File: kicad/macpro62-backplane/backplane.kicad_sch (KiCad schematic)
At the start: 0 parts

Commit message: Cross-board compatibility audit: interface control doc, CR-BP-1 applied, J2/J3 row-swap pinouts, 15-pin face AUX, fan header removed from backplane, CPU board i226/BT1 cleanup
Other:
- removed sheet Fan
- sheet CPU board link (J1 CPU-LINK card edge) ports: added IOB_USB_DN, IOB_USB_DP, MOD_I2C0_SCL, MOD_I2C0_SDA; removed none
- sheet Face P (primary) AUX link ports: added FACE_MOD_LED_N; removed none
- sheet Face S (secondary) AUX link ports: added FACE_MOD_LED_N; removed none
- sheet I/O board low-speed link ports: added IOB_INT_N, IOB_PRSNT_N, IOB_USB_DN, IOB_USB_DP; removed none
- sheet Management MCU (RP2350A) ports: added FACE_P_MOD_LED_N, FACE_S_MOD_LED_N, IOB_INT_N, IOB_PRSNT_N, MOD_I2C0_SCL, MOD_I2C0_SDA; removed FAN_PWM, FAN_TACH
- sheet Power input, standby rails, safety gate ports: added none; removed 11V_SB, 12V_MAIN
- note added: "Off-board links: J1 CPU-LINK (card edge from CPU board) | J2 PSU-IN | J3/J4 Face P/S AUX (GH15) | J6 IOB-LINK (fan via IOB CONN_C, no J5) | J7 M.2 OpenCore | J8 SWD | J9/J10 MCIO 124 to Face P/S (PCIe hub)"
- note removed: "Off-board links: J1 CPU-LINK (card edge from CPU board) | J2 PSU-IN | J3/J4 Face P/S AUX | J5 FAN | J6 IOB-LINK | J7 M.2 OpenCore | J8 SWD | J9/J10 MCIO 124 to Face P/S (PCIe hub)"

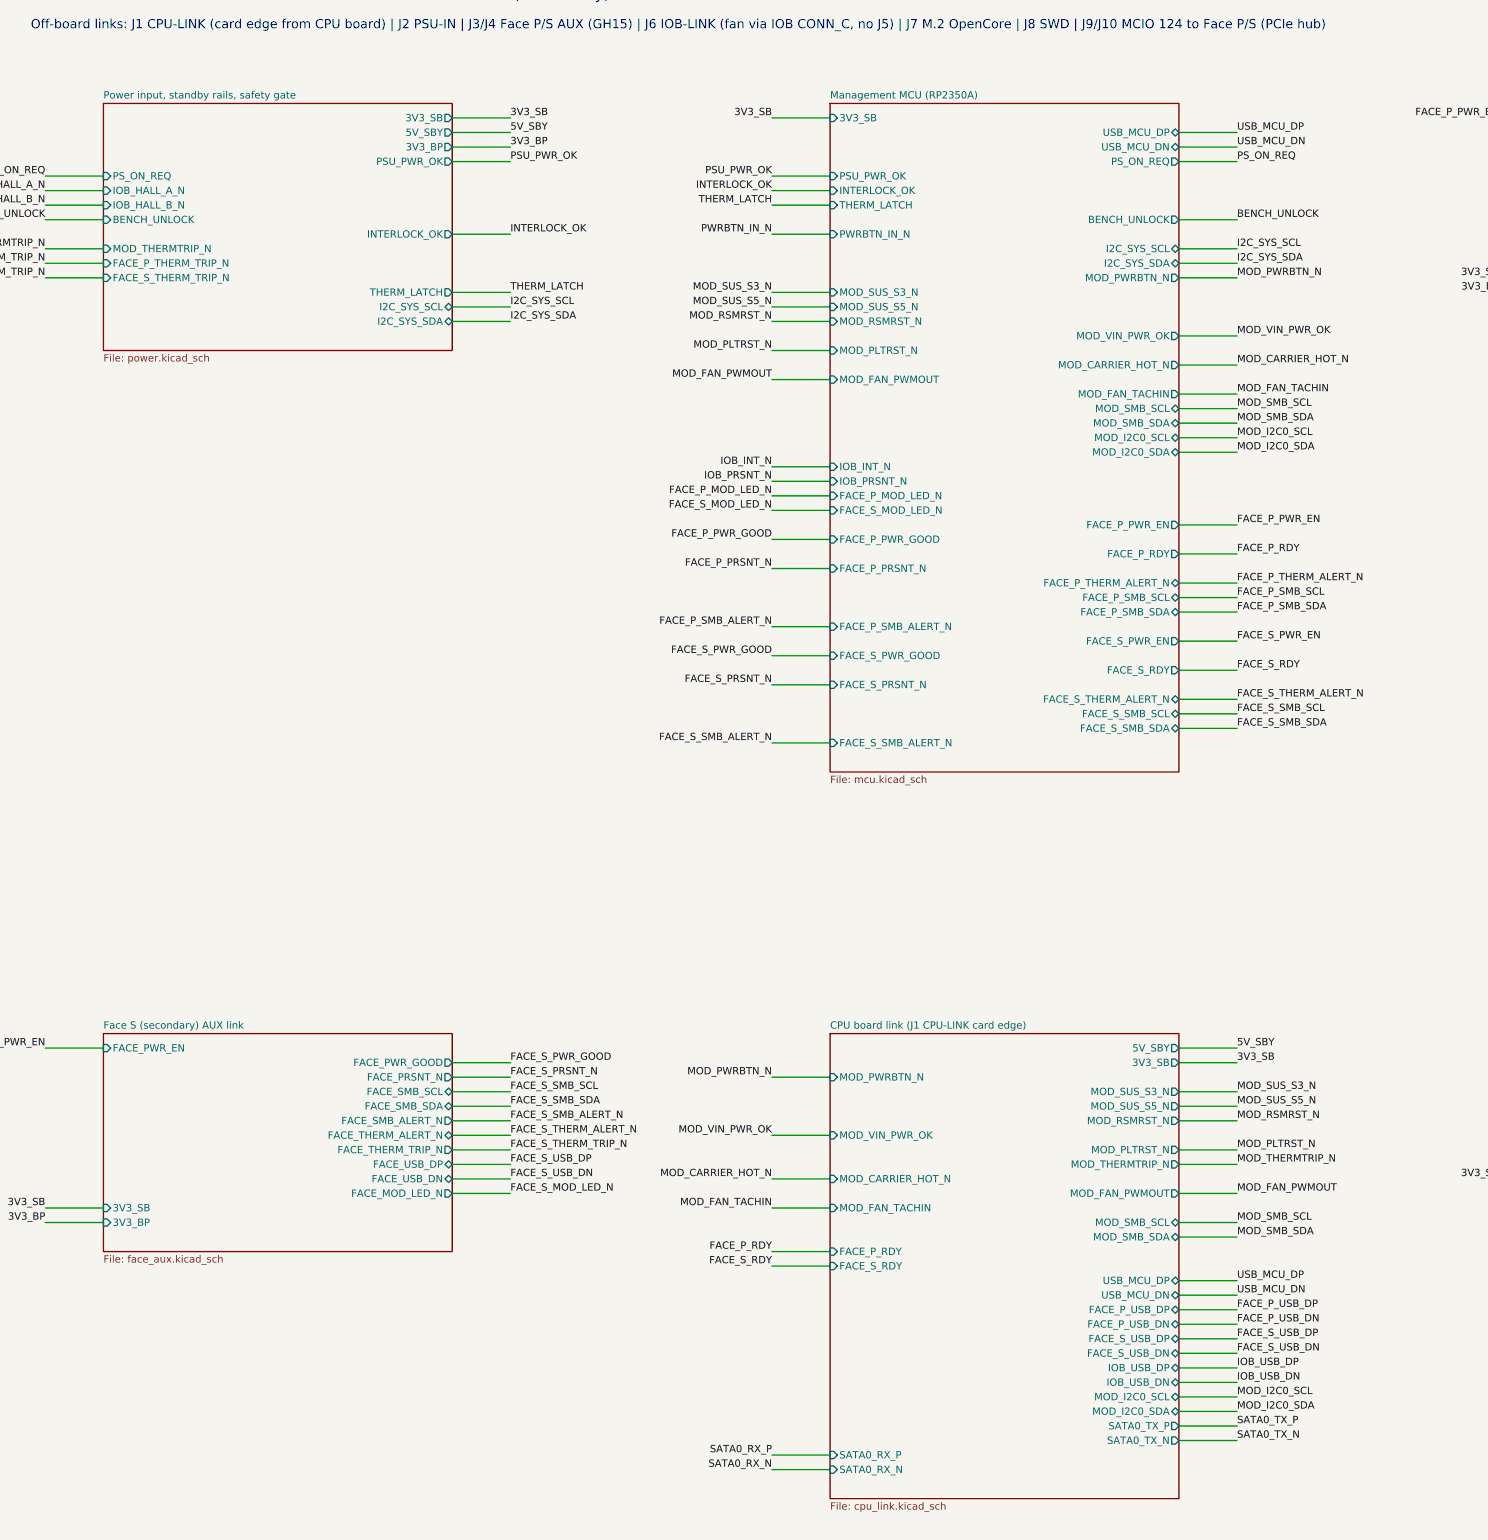
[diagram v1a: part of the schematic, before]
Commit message: ICD rev 2: 45 deg faces, 445 W ceiling + live power target (INA228 telemetry), ribbon MCIO jog cables, BT on S0, fan fail-safe, port-module I2C map
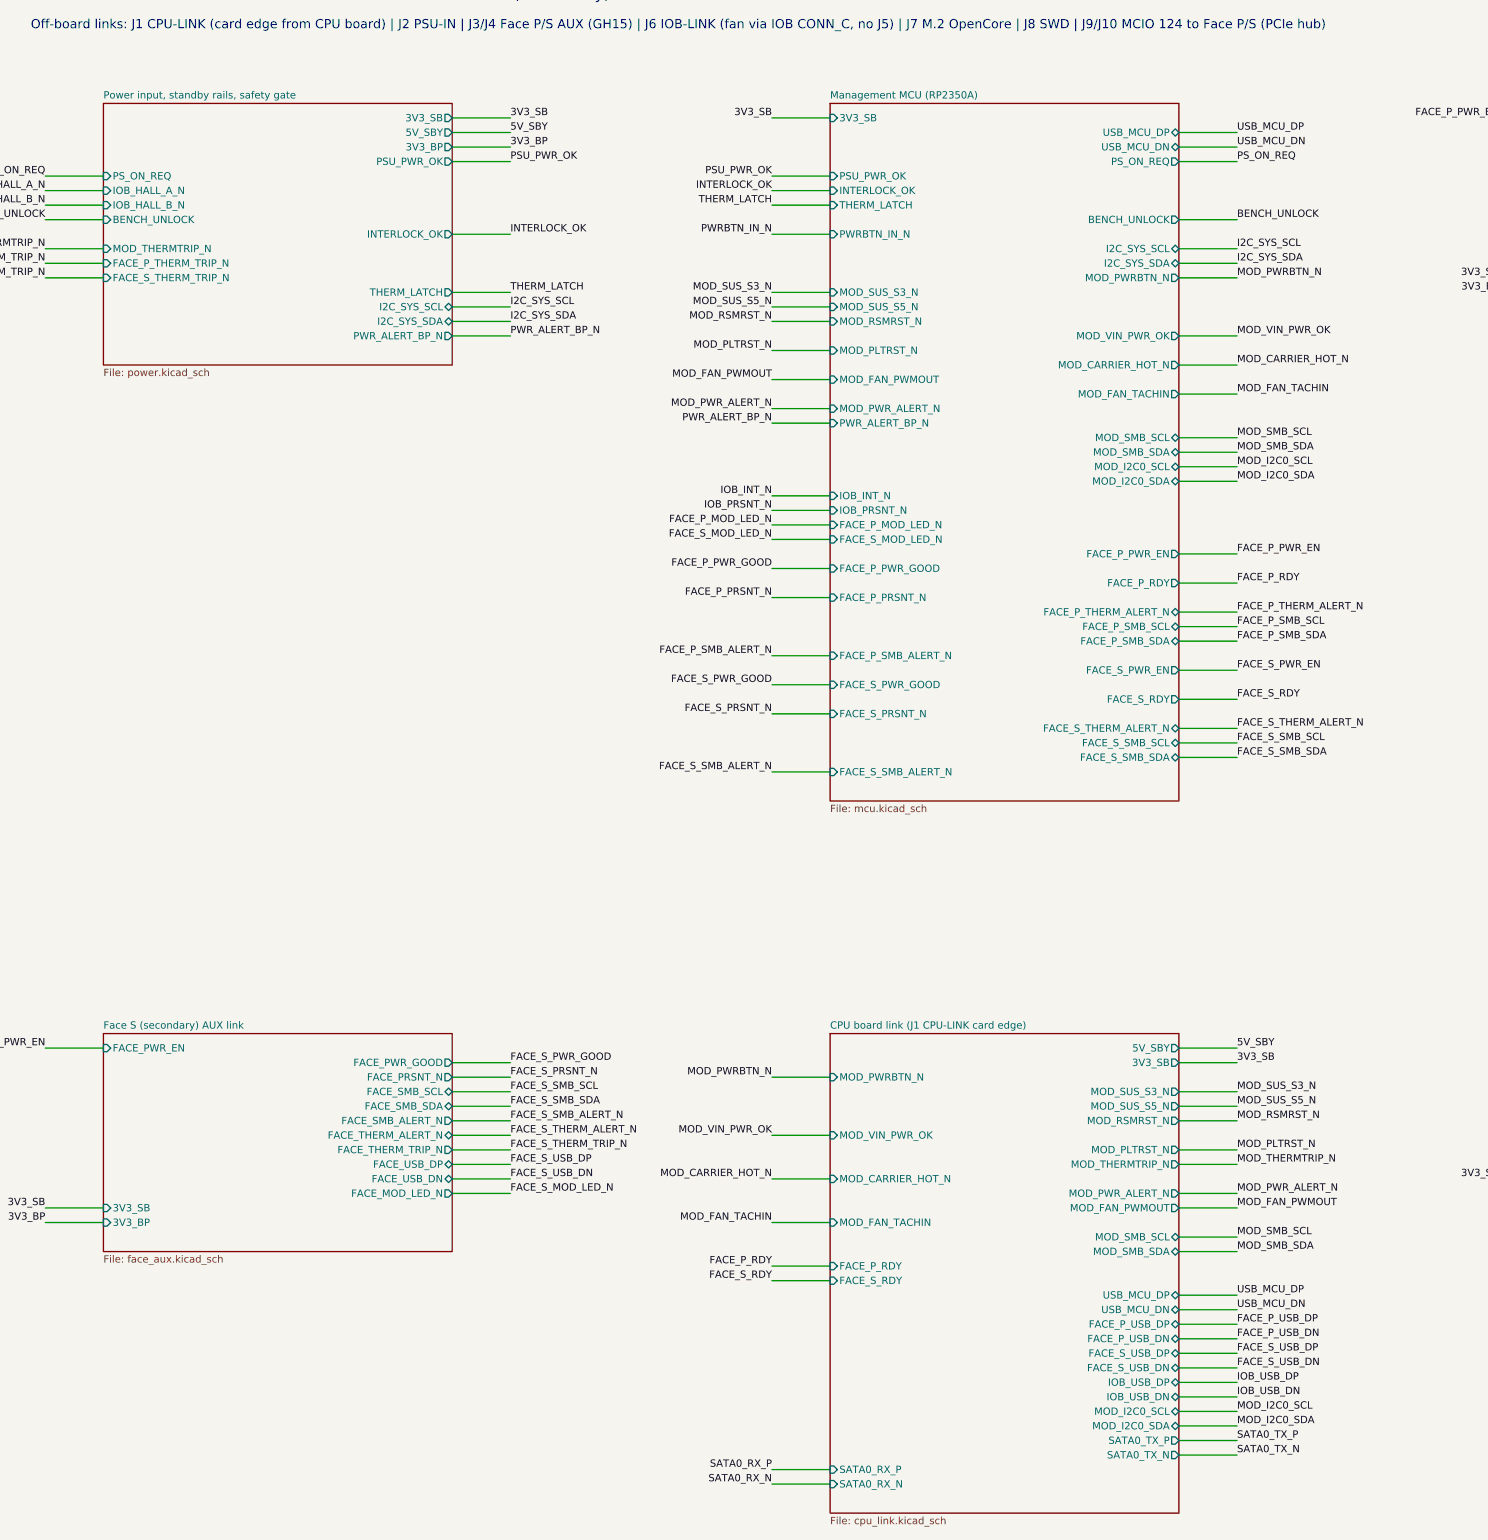
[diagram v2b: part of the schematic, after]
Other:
- sheet CPU board link (J1 CPU-LINK card edge) ports: added MOD_PWR_ALERT_N; removed none
- sheet Management MCU (RP2350A) ports: added MOD_PWR_ALERT_N, PWR_ALERT_BP_N; removed none
- sheet Power input, standby rails, safety gate ports: added PWR_ALERT_BP_N; removed none

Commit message: Backplane rev A1: 4-layer JLC04161H-7628, Gen5 redrivers removed, RP2350B MCU + INA226, fully routed (DRC/ERC 0, all HS/SATA pairs 0 skew), USB2 skew touch-up, JLC outputs
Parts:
- added C1, C12, C14, C16, C18, C19, C21, C22, C23, C24, C25, C26, C27, C28, C32, C33, C34, C35, C38, C39, C5, C8, C9: 100nF 16V X7R 0402, MP62_BP:C_0402_1005Metric, symbol MP62_BP:C
- added C10, C11, C13, C15, C17, C2, C3, C4, C6, C7: 22uF 25V X5R 0805, MP62_BP:C_0805_2012Metric, symbol MP62_BP:C
- added C20: 1uF 25V X5R 0402, MP62_BP:C_0402_1005Metric, symbol MP62_BP:C
- added C29, C30, C31: 4.7uF 10V X5R 0402, MP62_BP:C_0402_1005Metric, symbol MP62_BP:C
- added C36, C37: 15pF 50V C0G 0402, MP62_BP:C_0402_1005Metric, symbol MP62_BP:C
- added D1, D2: SS34 3A 40V Schottky SMA, MP62_BP:D_SMA, symbol MP62_BP:D
- added D10, D6, D7, D8, D9: LED red 0603, MP62_BP:LED_0603_1608Metric, symbol MP62_BP:LED
- added D3: SMAJ15A TVS SMA, MP62_BP:D_SMA, symbol MP62_BP:D
- added D4, D5: BAT54A (LBAT54ALT1G), MP62_BP:SOT-23, symbol MP62_BP:D_x2_ACom
- added F1: 3A 1206 fast fuse (0466003.NRHF class), MP62_BP:Fuse_1206_3216Metric, symbol MP62_BP:F
- added H1, H2: MountingHole D4 plated (GND), MP62_BP:MountingHole_4mm_Pad, symbol MP62_BP:HOLE
- added H3: M.2 2242 standoff pad (DNP option), MP62_BP:MP62_M2_Standoff_SMT_M2_Pad5.0, symbol MP62_BP:HOLE
- added J1: ME1022410103011 Mini Cool Edge 224 (C4941560, 0 s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, MP62_BP:MP62_CPULINK_MiniCoolEdge_224P_Vertical_SMT_PLACEHOLDER, symbol MP62_BP:CPULINK_224
- added J10: MCIO 124P RA (C4867471) -> Face S x4, MP62_BP:MP62_MCIO_124P_RA_SFF-TA-1016, symbol MP62_BP:MCIO124_BP
- added J2: Molex 43045-0812 Micro-Fit 2x4 (C277661), MP62_BP:Molex_Micro-Fit_3.0_43045-0812_2x04_P3.00mm_Vertical, symbol MP62_BP:MICROFIT8
- added J3: BM15B-GHS-TBT (C5305069) Face P AUX, MP62_BP:JST_GH_BM15B-GHS-TBT_1x15-1MP_P1.25mm_Vertical, symbol MP62_BP:GH15_AUX
- added J4: BM15B-GHS-TBT (C5305069) Face S AUX, MP62_BP:JST_GH_BM15B-GHS-TBT_1x15-1MP_P1.25mm_Vertical, symbol MP62_BP:GH15_AUX
- added J6: BM15B-GHS-TBT (C5305069) IOB-LINK, MP62_BP:JST_GH_BM15B-GHS-TBT_1x15-1MP_P1.25mm_Vertical, symbol MP62_BP:GH15_IOB
- added J7: M.2 M-key socket LOTES APCI0107 class (C841661) -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, MP62_BP:MP62_M2_MKey_SMT_H4.2_PLACEHOLDER, symbol MP62_BP:M2_M_SATA
- added J8: BM03B-SRSS-TB SWD (DNP), MP62_BP:JST_SH_BM03B-SRSS-TB_1x03-1MP_P1.00mm_Vertical, symbol MP62_BP:SH3_SWD
- added J9: MCIO 124P RA G97R24332HR class (C4867471, 0 stock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, MP62_BP:MP62_MCIO_124P_RA_SFF-TA-1016, symbol MP62_BP:MCIO124_BP
- added JP1: BENCH: bridges the Hall interlock (open = normal), MP62_BP:SolderJumper-2_P1.3mm_Open_RoundedPad1.0x1.5mm, symbol MP62_BP:JUMPER
- added L1, L2: 4.7uH 2A 4x4 (SWPA4030S4R7MT), MP62_BP:L_Changjiang_FNR4030S, symbol MP62_BP:L
- added L3: 3.3uH 0806 (FNR201610S3R3MT, RP2350 VREG), MP62_BP:L_0805_2012Metric, symbol MP62_BP:L
- added Q1, Q2, Q3, Q5, Q6, Q7, Q8: AO3401A P-MOS, MP62_BP:SOT-23, symbol MP62_BP:PMOS
- added Q10, Q11, Q4, Q9: 2N7002 N-MOS, MP62_BP:SOT-23, symbol MP62_BP:NMOS
- added R1: 33k 1% 0402, MP62_BP:R_0402_1005Metric, symbol MP62_BP:R
- added R10, R13, R14, R15, R16, R17, R18, R19, R2, R20, R21, R23, R24, R25, R26, R29, R30, R33, R34, R35, R36, R39, R4, R40, R42, R43, R44, R45, R46, R47, R48, R49, R7, R8, R9: 10k 1% 0402, MP62_BP:R_0402_1005Metric, symbol MP62_BP:R
- added R100: 10mR 1% 1W 1206 shunt, MP62_BP:R_1206_3216Metric, symbol MP62_BP:R
- added R11, R12, R55: 100k 1% 0402, MP62_BP:R_0402_1005Metric, symbol MP62_BP:R
- added R22, R31, R32, R41, R54, R58, R60, R61: 1k 1% 0402, MP62_BP:R_0402_1005Metric, symbol MP62_BP:R
- added R27, R28, R37, R38, R50, R51, R52, R53: 2.2k 1% 0402, MP62_BP:R_0402_1005Metric, symbol MP62_BP:R
- added R3: 56k 1% 0402, MP62_BP:R_0402_1005Metric, symbol MP62_BP:R
- added R5: 100k 1% 0402 (U6 EN, always on), MP62_BP:R_0402_1005Metric, symbol MP62_BP:R
- added R56: 10k 1% 0402 (12V LED), MP62_BP:R_0402_1005Metric, symbol MP62_BP:R
- added R57: 10k 1% 0402 (11V_SB LED), MP62_BP:R_0402_1005Metric, symbol MP62_BP:R
- added R59, R62, R63: 33R 1% 0402, MP62_BP:R_0402_1005Metric, symbol MP62_BP:R
- added R6: 100k 1% 0402 (U7 off until the MCU enables 5V_SBY), MP62_BP:R_0402_1005Metric, symbol MP62_BP:R
- added SW1: BOOTSEL (TS-1187A), MP62_BP:SW_Push_1P1T_XKB_TS-1187A, symbol MP62_BP:SW
- added SW2: BENCH power button (TS-1187A), MP62_BP:SW_Push_1P1T_XKB_TS-1187A, symbol MP62_BP:SW
- added U1: RP2350B QFN-80 (C42415655), MP62_BP:QFN-80-1EP_10x10mm_P0.4mm_EP3.4x3.4mm, symbol MP62_BP:RP2350B
- added U2: W25Q128JVSIQ (C97521, basic), MP62_BP:SOIC-8_5.3x5.3mm_P1.27mm, symbol MP62_BP:W25Q_SOIC8
- added U3: TMP1075DGKR @0x48 core side (C2864807), MP62_BP:VSSOP-8_3x3mm_P0.65mm, symbol MP62_BP:TMP1075_DGK
- added U4: TMP1075DGKR @0x49 PSU side (C2864807), MP62_BP:VSSOP-8_3x3mm_P0.65mm, symbol MP62_BP:TMP1075_DGK
- added U5: INA226AIDGSR @0x40 (C49851), MP62_BP:VSSOP-10_3x3mm_P0.5mm, symbol MP62_BP:INA226
- added U6: TPS563201DDCR (C116592) -> 3V3_SB, MP62_BP:SOT-23-6, symbol MP62_BP:TPS563201
- added U7: TPS563201DDCR (C116592) -> 5V_SBY, MP62_BP:SOT-23-6, symbol MP62_BP:TPS563201
- added U8: SN74LVC1G74DCUR thermal latch (C70285), MP62_BP:VSSOP-8_2.3x2mm_P0.5mm, symbol MP62_BP:LVC1G74
- added Y1: 12MHz 3225 crystal 20pF, MP62_BP:Crystal_SMD_3225-4Pin_3.2x2.5mm, symbol MP62_BP:XTAL4
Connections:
- net 3V3_SB: now also C1.1, C19.1, C21.1, C22.1, C23.1, C24.1, C25.1, C26.1, C27.1, C28.1, C29.1, C38.1, C6.1, C7.1, D10.2 (A), J1.B107 (3V3_SB), J1.B108 (3V3_SB), J6.1 (3V3_SB), J6.2 (3V3_SB), JP1.1, L1.2, Q1.2 (S), Q2.2 (S), Q3.2 (S), Q5.2 (S), Q6.2 (S), R1.1, R13.2, R14.2, R15.2, R16.2, R17.2, R18.2, R19.2, R20.2, R21.2, R23.2, R24.2, R25.2, R33.2, R34.2, R35.2, R42.2, R43.2, R44.2, R45.2, R46.2, R47.2, R48.2, R49.2, R50.2, R51.2, R52.2, R53.2, R59.1, R7.2, R8.2, R9.2, U1.15 (IOVDD), U1.24 (IOVDD), U1.29 (IOVDD), U1.41 (IOVDD), U1.5 (IOVDD), U1.50 (IOVDD), U1.59 (ADC_AVDD), U1.60 (IOVDD), U1.64 (VREG_VIN), U1.68 (USB_OTP_VDD), U1.69 (QSPI_IOVDD), U1.76 (IOVDD), U2.8 (VCC), U3.8 (V+), U4.7 (A0), U4.8 (V+), U5.6 (VS), U8.8 (VCC)
- net 5V_SBY: now also C10.1, C11.1, J1.A107 (5V_SBY), J1.A108 (5V_SBY), J1.A110 (5V_SBY), J1.A111 (5V_SBY), J1.B110 (5V_SBY), J1.B111 (5V_SBY), L2.2, R3.1
- net I2C_SYS_SCL: now also J6.8 (I2C_SYS_SCL), R52.1, U1.46 (GPIO37), U3.2 (SCL), U4.2 (SCL), U5.5 (SCL)
- net I2C_SYS_SDA: now also J6.9 (I2C_SYS_SDA), R53.1, U1.45 (GPIO36), U3.1 (SDA), U4.1 (SDA), U5.4 (SDA)
- net IOB_PRSNT_N: now also J6.11 (IOB_PRSNT_N), R48.1, U1.22 (GPIO22)
- net PSU_PWR_OK: now also J2.8 (PWR_OK), R54.1
- net PWRBTN_IN_N: now also J6.4 (PWRBTN_IN_N), R49.1, SW2.1, U1.25 (GPIO24)
- net SATA0_RX_N: now also J1.B71 (SATA0_RX_N), J7.43 (SATA-B-(HRX-))
- net SATA0_RX_P: now also J1.B70 (SATA0_RX_P), J7.41 (SATA-B+(HRX+))
- net SATA0_TX_N: now also J1.A74 (SATA0_TX_N), J7.47 (SATA-A-(HTX-))
- net SATA0_TX_P: now also J1.A73 (SATA0_TX_P), J7.49 (SATA-A+(HTX+))
- net THERM_LATCH: now also Q8.1 (G), U1.27 (GPIO26), U8.5 (Q)
- new net 11V_SB_IN: D2.2 (A), D9.2 (A), J2.7 (11V_SB)
- new net 12V_MAIN_IN: D1.2 (A), D8.2 (A), J2.1 (12V_MAIN), J2.2 (12V_MAIN)
- new net 3V3_AUX_P: C13.1, C14.1, J3.1 (3V3_AUX), J3.2 (3V3_AUX), Q1.3 (D), R26.2, R27.2, R28.2, R29.2, R30.2, R31.2
- new net 3V3_AUX_S: C15.1, C16.1, J4.1 (3V3_AUX), J4.2 (3V3_AUX), Q2.3 (D), R36.2, R37.2, R38.2, R39.2, R40.2, R41.2
- new net 3V3_M2: C17.1, C18.1, J7.12 (3V3), J7.14 (3V3), J7.16 (3V3), J7.18 (3V3), J7.2 (3V3), J7.4 (3V3), J7.70 (3V3), J7.72 (3V3), J7.74 (3V3), Q3.3 (D)
- new net AUXP_EN_N: Q1.1 (G), R7.1, U1.37 (GPIO29)
- new net AUXS_EN_N: Q2.1 (G), R8.1, U1.19 (GPIO19)
- new net BOOTSEL_N: R61.2, SW1.1
- new net BP_OTEMP_N: D5.2 (K2), R21.1, U3.3 (ALERT), U4.3 (ALERT)
- new net BST_3V3_SB: C5.1, U6.6 (VBST)
- new net BST_5V_SBY: C9.1, U7.6 (VBST)
- new net CB_CARRIER_HOT_N: J1.A98 (CARRIER_HOT#), R44.1, U1.13 (GPIO14)
- new net CB_FAN_PWM: J1.B96 (FAN_PWMOUT), U1.6 (GPIO8)
- new net CB_FAN_TACH: J1.B98 (FAN_TACHIN), U1.2 (GPIO5)
- new net CB_I2C0_SCL: J1.B90 (I2C0_CLK), R50.1, U1.80 (GPIO3)
- new net CB_I2C0_SDA: J1.B92 (I2C0_DAT), R51.1, U1.79 (GPIO2)
- new net CB_PLTRST_N: J1.A95 (PLTRST#), R22.1, R32.1, U1.54 (GPIO43)
- new net CB_PWRBTN_N: J1.A86 (PWRBTN#), R42.1, U1.57 (GPIO46)
- new net CB_PWR_ALERT_N: J1.A105 (PWR_ALERT#), R43.1, U1.12 (GPIO13)
- new net CB_RSMRST_N: J1.A92 (RSMRST_OUT#), U1.16 (GPIO16)
- new net CB_SUS_S3_N: J1.A89 (SUS_S3#), Q4.1 (G), U1.21 (GPIO21)
- new net CB_SUS_S45_N: J1.A90 (SUS_S4_S5#), U1.58 (GPIO47)
- new net CB_THERMTRIP_N: D4.1 (K1), J1.A96 (THERMTRIP#), R18.1
- new net CB_UART0_RX: J1.B95 (UART0_RX), U1.78 (GPIO1)
- new net CB_UART0_TX: J1.B93 (UART0_TX), U1.77 (GPIO0)
- new net CB_VIN_PWR_OK: J1.A93 (VIN_PWR_OK), U1.14 (GPIO15)
- new net CC_PRSNT1_N: J1.A1 (CC_PRSNT1#), R45.1, U1.53 (GPIO42)
- new net CC_PRSNT2_N: J1.A112 (CC_PRSNT2#), R46.1, U1.11 (GPIO12)
- new net DVDD: C30.1, C31.1, C32.1, C33.1, C34.1, L3.2, U1.10 (DVDD), U1.32 (DVDD), U1.51 (DVDD), U1.65 (VREG_FB)
- new net EN_3V3: R5.1, U6.5 (EN)
- new net EN_5V: R6.1, U1.40 (GPIO32), U7.5 (EN)
- new net FB_3V3_SB: R1.2, R2.1, U6.4 (VFB)
- new net FB_5V_SBY: R3.2, R4.1, U7.4 (VFB)
- new net FP_HOLD: Q10.1 (G), R23.1, U1.36 (GPIO28)
- new net FP_LEDA: D6.2 (A), R31.1
- new net FP_MCIO_PRSNT_N: J9.B12 (PRSNT), R24.1, U1.47 (GPIO38)
- new net FP_MOD_LED_N: D6.1 (K), J3.15 (MOD_LED#)
- new net FP_PERST_N: J9.B11 (PERST), Q10.3 (D), R22.2
- new net FP_PRSNT_N: J3.4 (FACE_PRSNT#), R25.1, U1.42 (GPIO33)
- new net FP_PWR_EN: J3.5 (FACE_PWR_EN), U1.49 (GPIO40_ADC0)
- new net FP_PWR_GOOD: J3.6 (FACE_PWR_GOOD), R26.1, U1.43 (GPIO34)
- new net FP_REFCLK_N: J1.A52 (FP_REFCLK_N), J9.A12 (REFCLK-)
- new net FP_REFCLK_P: J1.A51 (FP_REFCLK_P), J9.A11 (REFCLK+)
- new net FP_RX0_N: J1.B49 (FP_PER0_N), J9.A3 (PER0N)
- new net FP_RX0_P: J1.B48 (FP_PER0_P), J9.A2 (PER0P)
- new net FP_RX10_N: J1.B18 (FP_PER10_N), J9.A46 (PER10N)
- new net FP_RX10_P: J1.B17 (FP_PER10_P), J9.A45 (PER10P)
- new net FP_RX11_N: J1.B15 (FP_PER11_N), J9.A49 (PER11N)
- new net FP_RX11_P: J1.B14 (FP_PER11_P), J9.A48 (PER11P)
- new net FP_RX12_N: J1.B12 (FP_PER12_N), J9.A52 (PER12N)
- new net FP_RX12_P: J1.B11 (FP_PER12_P), J9.A51 (PER12P)
- new net FP_RX13_N: J1.B9 (FP_PER13_N), J9.A55 (PER13N)
- new net FP_RX13_P: J1.B8 (FP_PER13_P), J9.A54 (PER13P)
- new net FP_RX14_N: J1.B6 (FP_PER14_N), J9.A58 (PER14N)
- new net FP_RX14_P: J1.B5 (FP_PER14_P), J9.A57 (PER14P)
- new net FP_RX15_N: J1.B3 (FP_PER15_N), J9.A61 (PER15N)
- new net FP_RX15_P: J1.B2 (FP_PER15_P), J9.A60 (PER15P)
- new net FP_RX1_N: J1.B46 (FP_PER1_N), J9.A6 (PER1N)
- new net FP_RX1_P: J1.B45 (FP_PER1_P), J9.A5 (PER1P)
- new net FP_RX2_N: J1.B43 (FP_PER2_N), J9.A15 (PER2N)
- new net FP_RX2_P: J1.B42 (FP_PER2_P), J9.A14 (PER2P)
- new net FP_RX3_N: J1.B40 (FP_PER3_N), J9.A18 (PER3N)
- new net FP_RX3_P: J1.B39 (FP_PER3_P), J9.A17 (PER3P)
- new net FP_RX4_N: J1.B37 (FP_PER4_N), J9.A21 (PER4N)
- new net FP_RX4_P: J1.B36 (FP_PER4_P), J9.A20 (PER4P)
- new net FP_RX5_N: J1.B34 (FP_PER5_N), J9.A24 (PER5N)
- new net FP_RX5_P: J1.B33 (FP_PER5_P), J9.A23 (PER5P)
- new net FP_RX6_N: J1.B31 (FP_PER6_N), J9.A33 (PER6N)
- new net FP_RX6_P: J1.B30 (FP_PER6_P), J9.A32 (PER6P)
- new net FP_RX7_N: J1.B27 (FP_PER7_N), J9.A36 (PER7N)
- new net FP_RX7_P: J1.B26 (FP_PER7_P), J9.A35 (PER7P)
- new net FP_RX8_N: J1.B24 (FP_PER8_N), J9.A40 (PER8N)
- new net FP_RX8_P: J1.B23 (FP_PER8_P), J9.A39 (PER8P)
- new net FP_RX9_N: J1.B21 (FP_PER9_N), J9.A43 (PER9N)
- new net FP_RX9_P: J1.B20 (FP_PER9_P), J9.A42 (PER9P)
- new net FP_SMB_ALERT_N: J3.10 (FACE_SMB_ALERT#), R29.1, U1.44 (GPIO35)
- new net FP_SMB_SCL: J3.8 (FACE_SMB_CLK), R27.1, U1.56 (GPIO45)
- new net FP_SMB_SDA: J3.9 (FACE_SMB_DAT), R28.1, U1.55 (GPIO44)
- new net FP_THERM_ALERT_N: J3.11 (THERM_ALERT#), R30.1, U1.23 (GPIO23)
- new net FP_THERM_TRIP_N: D4.2 (K2), J3.12 (THERM_TRIP#), R19.1
- new net FP_TX0_N: J1.A49 (FP_PET0_N), J9.B3 (PET0N)
- new net FP_TX0_P: J1.A48 (FP_PET0_P), J9.B2 (PET0P)
- new net FP_TX10_N: J1.A18 (FP_PET10_N), J9.B46 (PET10N)
- new net FP_TX10_P: J1.A17 (FP_PET10_P), J9.B45 (PET10P)
- new net FP_TX11_N: J1.A15 (FP_PET11_N), J9.B49 (PET11N)
- new net FP_TX11_P: J1.A14 (FP_PET11_P), J9.B48 (PET11P)
- new net FP_TX12_N: J1.A12 (FP_PET12_N), J9.B52 (PET12N)
- new net FP_TX12_P: J1.A11 (FP_PET12_P), J9.B51 (PET12P)
- new net FP_TX13_N: J1.A9 (FP_PET13_N), J9.B55 (PET13N)
- new net FP_TX13_P: J1.A8 (FP_PET13_P), J9.B54 (PET13P)
- new net FP_TX14_N: J1.A6 (FP_PET14_N), J9.B58 (PET14N)
- new net FP_TX14_P: J1.A5 (FP_PET14_P), J9.B57 (PET14P)
- new net FP_TX15_N: J1.A3 (FP_PET15_N), J9.B61 (PET15N)
- new net FP_TX15_P: J1.A2 (FP_PET15_P), J9.B60 (PET15P)
- new net FP_TX1_N: J1.A46 (FP_PET1_N), J9.B6 (PET1N)
- new net FP_TX1_P: J1.A45 (FP_PET1_P), J9.B5 (PET1P)
- new net FP_TX2_N: J1.A43 (FP_PET2_N), J9.B15 (PET2N)
- new net FP_TX2_P: J1.A42 (FP_PET2_P), J9.B14 (PET2P)
- new net FP_TX3_N: J1.A40 (FP_PET3_N), J9.B18 (PET3N)
- new net FP_TX3_P: J1.A39 (FP_PET3_P), J9.B17 (PET3P)
- new net FP_TX4_N: J1.A37 (FP_PET4_N), J9.B21 (PET4N)
- new net FP_TX4_P: J1.A36 (FP_PET4_P), J9.B20 (PET4P)
- new net FP_TX5_N: J1.A34 (FP_PET5_N), J9.B24 (PET5N)
- new net FP_TX5_P: J1.A33 (FP_PET5_P), J9.B23 (PET5P)
- new net FP_TX6_N: J1.A31 (FP_PET6_N), J9.B33 (PET6N)
- new net FP_TX6_P: J1.A30 (FP_PET6_P), J9.B32 (PET6P)
- new net FP_TX7_N: J1.A27 (FP_PET7_N), J9.B36 (PET7N)
- new net FP_TX7_P: J1.A26 (FP_PET7_P), J9.B35 (PET7P)
- new net FP_TX8_N: J1.A24 (FP_PET8_N), J9.B40 (PET8N)
- new net FP_TX8_P: J1.A23 (FP_PET8_P), J9.B39 (PET8P)
- new net FP_TX9_N: J1.A21 (FP_PET9_N), J9.B43 (PET9N)
- new net FP_TX9_P: J1.A20 (FP_PET9_P), J9.B42 (PET9P)
- new net FS_HOLD: Q11.1 (G), R33.1, U1.17 (GPIO17)
- new net FS_LEDA: D7.2 (A), R41.1
- new net FS_MCIO_PRSNT_N: J10.B12 (PRSNT), R34.1, U1.8 (GPIO10)
- new net FS_MOD_LED_N: D7.1 (K), J4.15 (MOD_LED#)
- new net FS_PERST_N: J10.B11 (PERST), Q11.3 (D), R32.2
- new net FS_PRSNT_N: J4.4 (FACE_PRSNT#), R35.1, U1.9 (GPIO11)
- new net FS_PWR_EN: J4.5 (FACE_PWR_EN), U1.1 (GPIO4)
- new net FS_PWR_GOOD: J4.6 (FACE_PWR_GOOD), R36.1, U1.7 (GPIO9)
- new net FS_REFCLK_N: J1.A71 (FS_REFCLK_N), J10.A12 (REFCLK-)
- new net FS_REFCLK_P: J1.A70 (FS_REFCLK_P), J10.A11 (REFCLK+)
- new net FS_RX0_N: J1.B68 (FS_PER0_N), J10.A3 (PER0N)
- new net FS_RX0_P: J1.B67 (FS_PER0_P), J10.A2 (PER0P)
- new net FS_RX1_N: J1.B65 (FS_PER1_N), J10.A6 (PER1N)
- new net FS_RX1_P: J1.B64 (FS_PER1_P), J10.A5 (PER1P)
- new net FS_RX2_N: J1.B62 (FS_PER2_N), J10.A15 (PER2N)
- new net FS_RX2_P: J1.B61 (FS_PER2_P), J10.A14 (PER2P)
- new net FS_RX3_N: J1.B59 (FS_PER3_N), J10.A18 (PER3N)
- new net FS_RX3_P: J1.B58 (FS_PER3_P), J10.A17 (PER3P)
- new net FS_SMB_ALERT_N: J4.10 (FACE_SMB_ALERT#), R39.1, U1.52 (GPIO41)
- new net FS_SMB_SCL: J4.8 (FACE_SMB_CLK), R37.1, U1.4 (GPIO7)
- new net FS_SMB_SDA: J4.9 (FACE_SMB_DAT), R38.1, U1.3 (GPIO6)
- new net FS_THERM_ALERT_N: J4.11 (THERM_ALERT#), R40.1, U1.48 (GPIO39)
- new net FS_THERM_TRIP_N: D5.1 (K1), J4.12 (THERM_TRIP#), R20.1
- new net FS_TX0_N: J1.A68 (FS_PET0_N), J10.B3 (PET0N)
- new net FS_TX0_P: J1.A67 (FS_PET0_P), J10.B2 (PET0P)
- new net FS_TX1_N: J1.A65 (FS_PET1_N), J10.B6 (PET1N)
- new net FS_TX1_P: J1.A64 (FS_PET1_P), J10.B5 (PET1P)
- new net FS_TX2_N: J1.A62 (FS_PET2_N), J10.B15 (PET2N)
- new net FS_TX2_P: J1.A61 (FS_PET2_P), J10.B14 (PET2P)
- new net FS_TX3_N: J1.A59 (FS_PET3_N), J10.B18 (PET3N)
- new net FS_TX3_P: J1.A58 (FS_PET3_P), J10.B17 (PET3P)
- new net GND: C1.2, C10.2, C11.2, C12.2, C13.2, C14.2, C15.2, C16.2, C17.2, C18.2, C19.2, C2.2, C20.2, C21.2, C22.2, C23.2, C24.2, C25.2, C26.2, C27.2, C28.2, C29.2, C3.2, C30.2, C31.2, C32.2, C33.2, C34.2, C35.2, C36.2, C37.2, C38.2, C39.2, C4.2, C6.2, C7.2, C8.2, D3.2 (A), H1.1, H2.1, H3.1, J1.A10 (GND), J1.A100 (GND), J1.A103 (GND), J1.A106 (GND), J1.A109 (GND), J1.A13 (GND), J1.A16 (GND), J1.A19 (GND), J1.A22 (GND), J1.A25 (GND), J1.A28 (GND), J1.A29 (GND), J1.A32 (GND), J1.A35 (GND), J1.A38 (GND), J1.A4 (GND), J1.A41 (GND), J1.A44 (GND), J1.A47 (GND), J1.A50 (GND), J1.A53 (GND), J1.A56 (GND), J1.A57 (GND), J1.A60 (GND), J1.A63 (GND), J1.A66 (GND), J1.A69 (GND), J1.A7 (GND), J1.A72 (GND), J1.A75 (GND), J1.A78 (GND), J1.A81 (GND), J1.A82 (GND), J1.A83 (GND), J1.A84 (GND), J1.A85 (GND), J1.A88 (GND), J1.A91 (GND), J1.A94 (GND), J1.A97 (GND), J1.B1 (GND), J1.B10 (GND), J1.B100 (GND), J1.B103 (GND), J1.B106 (GND), J1.B109 (GND), J1.B112 (GND), J1.B13 (GND), J1.B16 (GND), J1.B19 (GND), J1.B22 (GND), J1.B25 (GND), J1.B28 (GND), J1.B29 (GND), J1.B32 (GND), J1.B35 (GND), J1.B38 (GND), J1.B4 (GND), J1.B41 (GND), J1.B44 (GND), J1.B47 (GND), J1.B50 (GND), J1.B53 (GND), J1.B56 (GND), J1.B57 (GND), J1.B60 (GND), J1.B63 (GND), J1.B66 (GND), J1.B69 (GND), J1.B7 (GND), J1.B72 (GND), J1.B75 (GND), J1.B78 (GND), J1.B81 (GND), J1.B84 (GND), J1.B85 (GND), J1.B88 (GND), J1.B91 (GND), J1.B94 (GND), J1.B97 (GND), J1.BL (BOARDLOCK), J10.A1 (GND), J10.A10 (GND), J10.A13 (GND), J10.A16 (GND), J10.A19 (GND), J10.A22 (GND), J10.A25 (GND), J10.A28 (GND), J10.A31 (GND), J10.A34 (GND), J10.A37 (GND), J10.A38 (GND), J10.A4 (GND), J10.A41 (GND), J10.A44 (GND), J10.A47 (GND), J10.A50 (GND), J10.A53 (GND), J10.A56 (GND), J10.A59 (GND), J10.A62 (GND), J10.A7 (GND), J10.B1 (GND), J10.B10 (GND), J10.B13 (GND), J10.B16 (GND), J10.B19 (GND), J10.B22 (GND), J10.B25 (GND), J10.B28 (GND), J10.B31 (GND), J10.B34 (GND), J10.B37 (GND), J10.B38 (GND), J10.B4 (GND), J10.B41 (GND), J10.B44 (GND), J10.B47 (GND), J10.B50 (GND), J10.B53 (GND), J10.B56 (GND), J10.B59 (GND), J10.B62 (GND), J10.B7 (GND), J10.MP (SHIELD), J2.3 (GND), J2.4 (GND), J2.5 (GND), J3.3 (GND), J3.7 (GND), J3.MP, J4.3 (GND), J4.7 (GND), J4.MP, J6.12 (GND), J6.15 (GND), J6.3 (GND), J6.7 (GND), J6.MP, J7.1 (GND), J7.15 (GND), J7.21 (GND), J7.27 (GND), J7.3 (GND), J7.33 (GND), J7.39 (GND), J7.45 (GND), J7.51 (GND), J7.57 (GND), J7.71 (GND), J7.73 (GND), J7.9 (GND), J7.MP, J8.2 (GND), J8.MP, J9.A1 (GND), J9.A10 (GND), J9.A13 (GND), J9.A16 (GND), J9.A19 (GND), J9.A22 (GND), J9.A25 (GND), J9.A28 (GND), J9.A31 (GND), J9.A34 (GND), J9.A37 (GND), J9.A38 (GND), J9.A4 (GND), J9.A41 (GND), J9.A44 (GND), J9.A47 (GND), J9.A50 (GND), J9.A53 (GND), J9.A56 (GND), J9.A59 (GND), J9.A62 (GND), J9.A7 (GND), J9.B1 (GND), J9.B10 (GND), J9.B13 (GND), J9.B16 (GND), J9.B19 (GND), J9.B22 (GND), J9.B25 (GND), J9.B28 (GND), J9.B31 (GND), J9.B34 (GND), J9.B37 (GND), J9.B38 (GND), J9.B4 (GND), J9.B41 (GND), J9.B44 (GND), J9.B47 (GND), J9.B50 (GND), J9.B53 (GND), J9.B56 (GND), J9.B59 (GND), J9.B62 (GND), J9.B7 (GND), J9.MP (SHIELD), Q10.2 (S), Q11.2 (S), Q4.2 (S), Q9.2 (S), R10.2, R11.2, R12.2, R2.2, R4.2, R55.2, R56.2, R57.2, R6.2, SW1.2, SW2.2, U1.62 (VREG_PGND), U1.81 (GND_EP), U2.4 (GND), U3.4 (GND), U3.5 (A2), U3.6 (A1), U3.7 (A0), U4.4 (GND), U4.5 (A2), U4.6 (A1), U5.1 (A1), U5.2 (A0), U5.7 (GND), U6.1 (GND), U7.1 (GND), U8.1 (CLK), U8.2 (D), U8.4 (GND), Y1.2 (GND), Y1.4 (GND)
- new net HALL_A_N: J6.5 (HALL_A_N), Q5.1 (G), R13.1
- new net HALL_B_N: J6.6 (HALL_B_N), Q6.1 (G), R14.1
- new net ILK_A: JP1.2, Q5.3 (D), Q6.3 (D), Q7.2 (S), R11.1, U1.38 (GPIO30)
- new net ILK_B: Q7.3 (D), Q8.2 (S)
- new net LATCH_CLR_N: C20.1, R16.1, U1.28 (GPIO27), U8.6 (CLR#)
- new net LED11_K: D9.1 (K), R57.1
- new net LED12_K: D8.1 (K), R56.1
- new net LED_ST_K: D10.1 (K), R58.1
- new net M2_DEVSLP: J7.38 (DEVSLP), R10.1
- new net M2_EN_N: Q3.1 (G), Q4.3 (D), R9.1
- new net MCU_LED_N: R58.2, U1.18 (GPIO18)
- new net MCU_RUN: C39.1, U1.35 (RUN)
- new net MCU_SWCLK: J8.1 (SWCLK), U1.33 (SWCLK)
- new net MCU_SWDIO: J8.3 (SWDIO), U1.34 (SWDIO)
- new net PSON_DRV: Q8.3 (D), Q9.1 (G), R12.1
- new net PSU_PS_ON_N: J2.6 (PS_ON#), Q9.3 (D)
- new net PSU_PWR_OK_M: R54.2, R55.1, U1.20 (GPIO20)
- new net PS_ON_REQ_N: Q7.1 (G), R15.1, U1.39 (GPIO31)
- new net QSPI_SCLK: U1.71 (QSPI_SCLK), U2.6 (CLK)
- new net QSPI_SD0: U1.72 (QSPI_SD0), U2.5 (DI(IO0))
- new net QSPI_SD1: U1.74 (QSPI_SD1), U2.2 (DO(IO1))
- new net QSPI_SD2: U1.73 (QSPI_SD2), U2.3 (WP#(IO2))
- new net QSPI_SD3: U1.70 (QSPI_SD3), U2.7 (HOLD#(IO3))
- new net QSPI_SS: R61.1, U1.75 (QSPI_SS), U2.1 (CS#)
- new net SW_3V3_SB: C5.2, L1.1, U6.2 (SW)
- new net SW_5V_SBY: C9.2, L2.1, U7.2 (SW)
- new net SYS_INT_N: J6.10 (IOB_INT_N), R47.1, U1.26 (GPIO25), U5.3 (ALERT)
- new net TRIP_N: D4.3 (A), D5.3 (A), R17.1, U8.7 (PRE#)
- new net USB2_FACEP_N: J1.B52 (USB2_FACEP_N), J3.14 (USB2_D-)
- new net USB2_FACEP_P: J1.B51 (USB2_FACEP_P), J3.13 (USB2_D+)
- new net USB2_FACES_N: J1.B77 (USB2_FACES_N), J4.14 (USB2_D-)
- new net USB2_FACES_P: J1.B76 (USB2_FACES_P), J4.13 (USB2_D+)
- new net USB2_MCU_N: J1.B74 (USB2_MCU_N), R63.2
- new net USB2_MCU_P: J1.B73 (USB2_MCU_P), R62.2
- new net USB2_SPARE_N: J1.B80 (USB2_SPARE_N), J6.14 (USB2_LINK_D-)
- new net USB2_SPARE_P: J1.B79 (USB2_SPARE_P), J6.13 (USB2_LINK_D+)
- new net USB_DM_M: R63.1, U1.66 (USB_DM)
- new net USB_DP_M: R62.1, U1.67 (USB_DP)
- new net VIN: C12.1, C2.1, C3.1, C4.1, C8.1, R100.2, R5.2, U5.8 (VBUS), U5.9 (IN-), U6.3 (VIN), U7.3 (VIN)
- new net VIN_F: D3.1 (K), F1.2, R100.1, U5.10 (IN+)
- new net VIN_OR: D1.1 (K), D2.1 (K), F1.1
- new net VREG_AVDD: C35.1, R59.2, U1.61 (VREG_AVDD)
- new net VREG_LX: L3.1, U1.63 (VREG_LX)
- new net XIN: C36.1, U1.30 (XIN), Y1.1 (X1)
- new net XOUT: R60.1, U1.31 (XOUT)
- new net XOUT_C: C37.1, R60.2, Y1.3 (X2)
- no-connect marks 0 -> 136
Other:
- removed sheet CPU board link (J1 CPU-LINK card edge)
- removed sheet Face P (primary) AUX link
- removed sheet Face S (secondary) AUX link
- removed sheet I/O board low-speed link
- removed sheet Management MCU (RP2350A)
- removed sheet OpenCore boot M.2 (SATA)
- removed sheet Power input, standby rails, safety gate
- note removed: "MP62 BACKPLANE rev A - BLOCK DIAGRAM. Sheets are stubs (labels only). Nets with the same label name are connected."
- note removed: "Off-board links: J1 CPU-LINK (card edge from CPU board) | J2 PSU-IN | J3/J4 Face P/S AUX (GH15) | J6 IOB-LINK (fan via IOB CONN_C, no J5) | J7 M.2 OpenCore | J8 SWD | J9/J10 MCIO 124 to Face P/S (PCIe hub)"
- title: MacPro6,2 Backplane (BP) - top-level block diagram -> MP62 backplane rev A1 (BP-G4 cost-down)
